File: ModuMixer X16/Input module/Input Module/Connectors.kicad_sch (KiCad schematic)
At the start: 4 parts, among them J1 Conn_01x03_Pin, J2 Conn_02x07_Counter_Clockwise, J3 Conn_02x07_Counter_Clockwise, J4 Conn_02x05_Counter_Clockwise

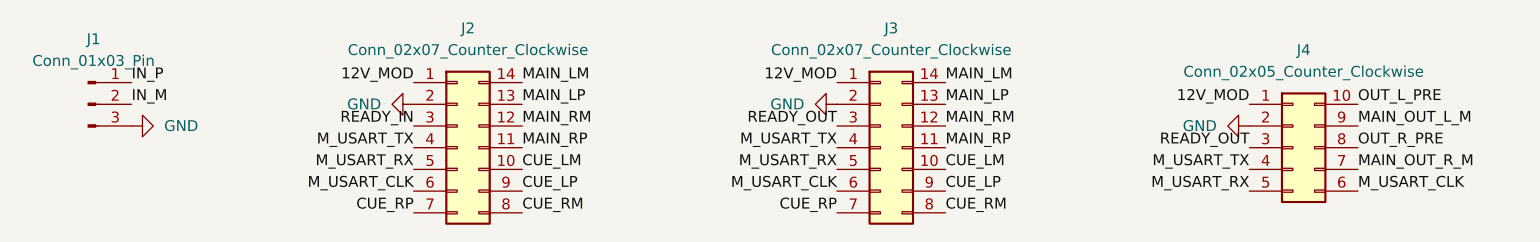
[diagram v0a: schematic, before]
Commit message: MCU replacement finished
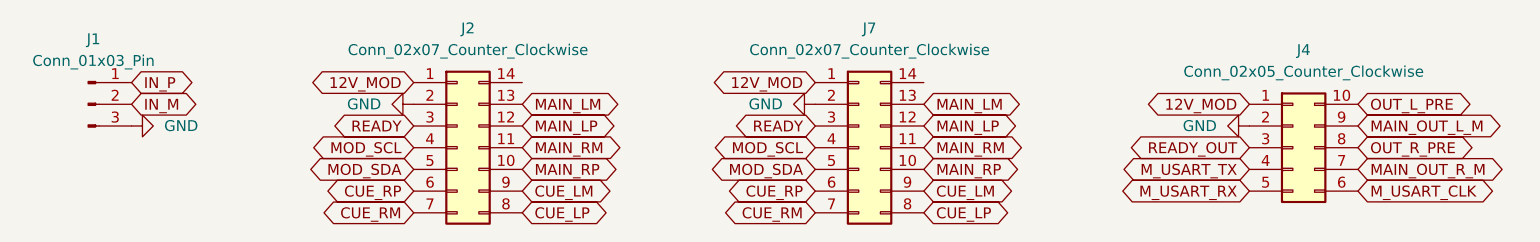
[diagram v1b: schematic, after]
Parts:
- removed J3: Conn_02x07_Counter_Clockwise, Connector_IDC:IDC-Header_2x07_P2.54mm_Vertical, symbol Connector_Generic:Conn_02x07_Counter_Clockwise
- added J7: Conn_02x07_Counter_Clockwise, Connector_IDC:IDC-Header_2x07_P2.54mm_Vertical, symbol Connector_Generic:Conn_02x07_Counter_Clockwise
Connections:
- net 12V_MOD: now also J7.1 (Pin_1)
- net CUE_LM: now also J2.9 (Pin_9), J7.9 (Pin_9); no longer J2.10 (Pin_10)
- net CUE_LP: now also J2.8 (Pin_8), J7.8 (Pin_8); no longer J2.9 (Pin_9)
- net CUE_RM: now also J2.7 (Pin_7), J7.7 (Pin_7); no longer J2.8 (Pin_8)
- net CUE_RP: now also J2.6 (Pin_6), J7.6 (Pin_6); no longer J2.7 (Pin_7)
- net GND: now also J7.2 (Pin_2)
- net MAIN_LM: now also J2.13 (Pin_13), J7.13 (Pin_13); no longer J2.14 (Pin_14)
- net MAIN_LP: now also J2.12 (Pin_12), J7.12 (Pin_12); no longer J2.13 (Pin_13)
- net MAIN_RM: now also J2.11 (Pin_11), J7.11 (Pin_11); no longer J2.12 (Pin_12)
- net MAIN_RP: now also J2.10 (Pin_10), J7.10 (Pin_10); no longer J2.11 (Pin_11)
- net M_USART_CLK: no longer J2.6 (Pin_6)
- net M_USART_RX: no longer J2.5 (Pin_5)
- net M_USART_TX: no longer J2.4 (Pin_4)
- net READY_IN renamed READY
- net READY: now also J7.3 (Pin_3)
- new net MOD_SCL: J2.4 (Pin_4), J7.4 (Pin_4)
- new net MOD_SDA: J2.5 (Pin_5), J7.5 (Pin_5)
